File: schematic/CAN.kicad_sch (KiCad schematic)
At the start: 7 parts, among them J3 TB006-508-03BE, U2 ISO1050DUBR

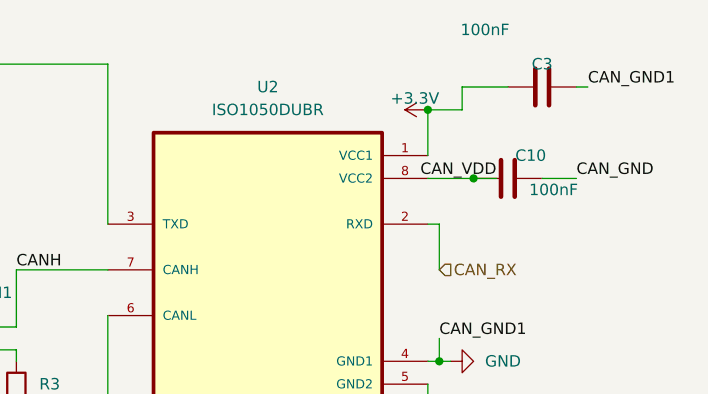
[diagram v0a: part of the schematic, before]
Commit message: Changed to Kicad Version 8
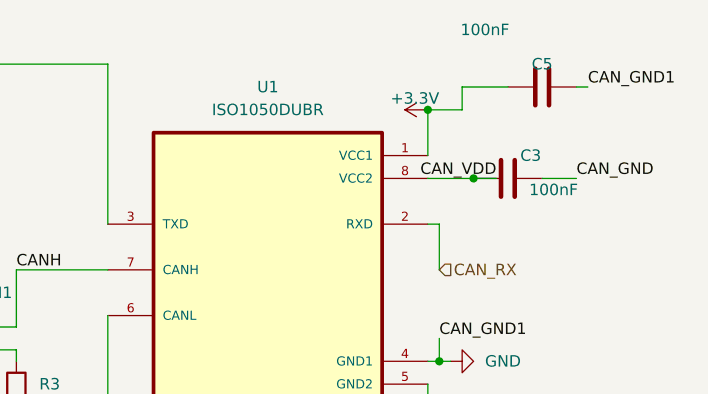
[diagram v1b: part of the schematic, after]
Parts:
- renumbered C10 to C3, C3 to C5, U2 to U1
